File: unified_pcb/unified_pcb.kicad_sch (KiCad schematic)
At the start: 102 parts, among them J1 Conn_01x02_Socket, J2 USB_C_Receptacle, J3 Conn_01x02_Socket, J4 Conn_01x03_Pin, Q1 Q_Photo_NPN, Q2 Q_Photo_NPN, Q3 Q_Photo_NPN, SW1 SW_Push, SW2 SW_Push, U1 BQ27427YZFR, U10 3.3V LDO, U11 LMD4030T261-OA1, U12 LY4176D, U2 USBLC6-2P6, U3 RS0302, U4 RP2350_60QFN, U5 TLV7113318DDSER, U7 QSPI Flash, U8 TPGLF72101CSP4, U9 ICM-20948, Y1 12MHz

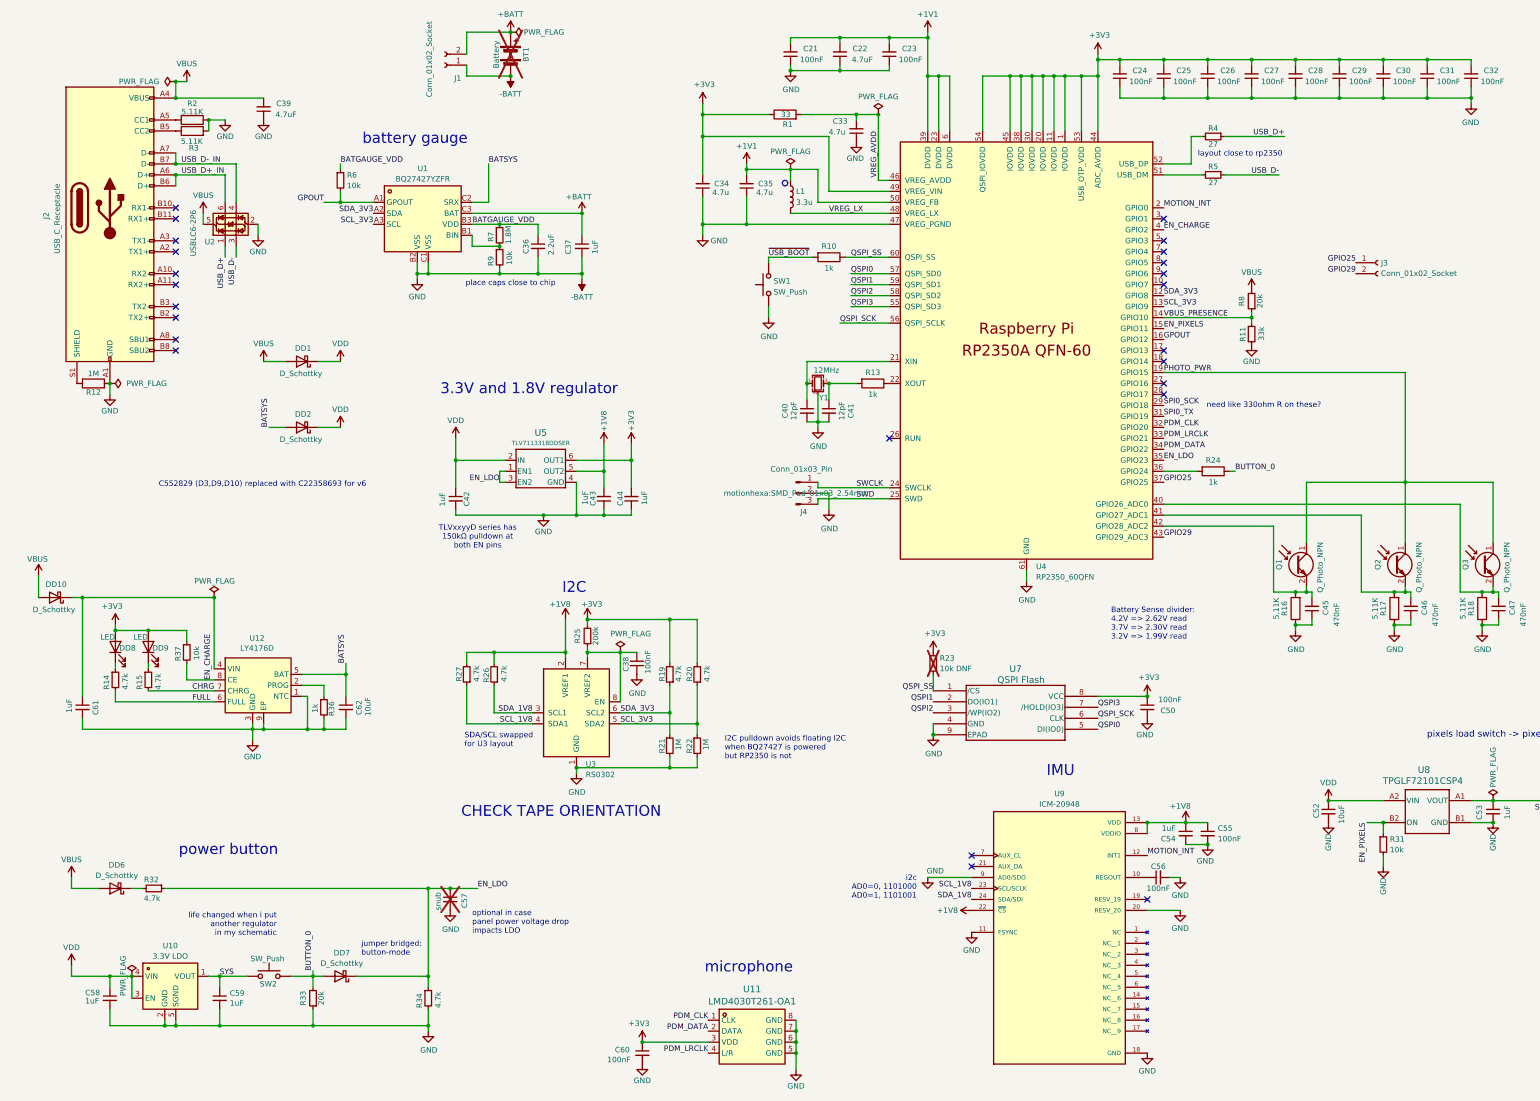
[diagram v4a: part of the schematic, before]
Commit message: wow ICM_20948 is moving out of production and is expensive - move to BMI270+MMC5603NJ, no need anymore for 1.8V net at all remove old schematic pieces, update schematic format mag layout fix crystal and other part nums
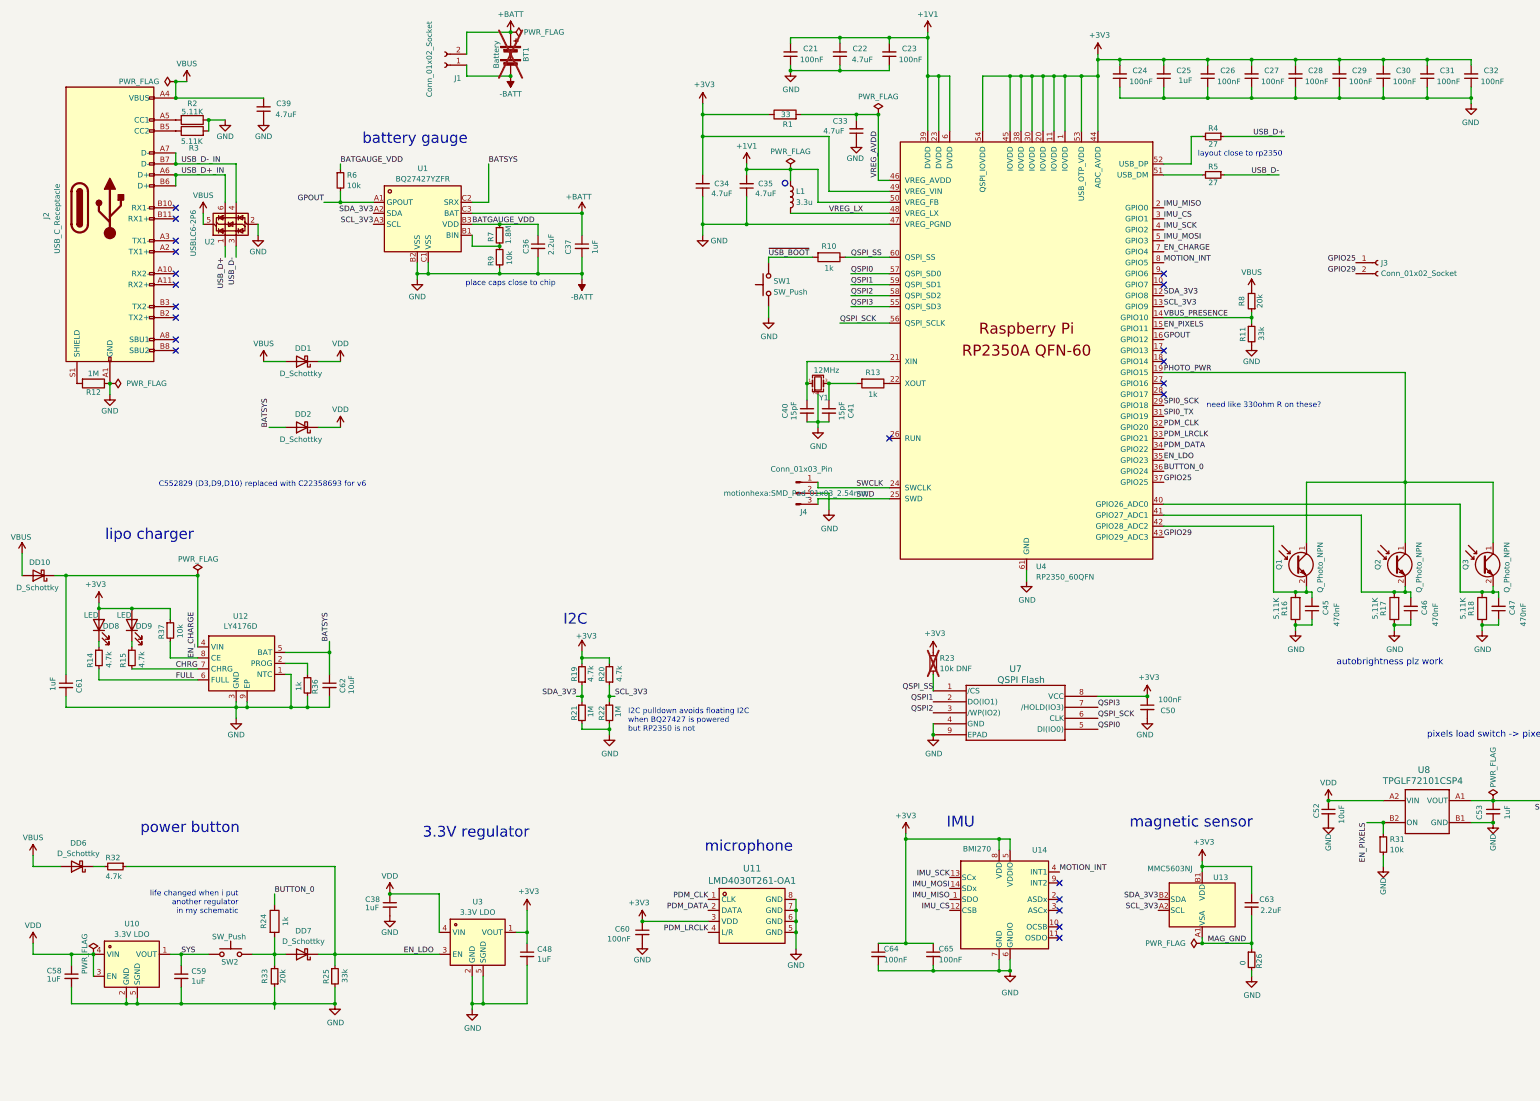
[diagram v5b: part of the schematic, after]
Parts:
- removed C42, C43, C44, C54: 1uF, Capacitor_SMD:C_0402_1005Metric, symbol Device:C_Small
- removed C55, C56: 100nF, Capacitor_SMD:C_0402_1005Metric, symbol Device:C_Small
- removed C57: snub, Capacitor_SMD:C_0402_1005Metric, symbol Device:C_Small
- removed R27, R34: 4.7k, Resistor_SMD:R_0402_1005Metric, symbol Device:R_Small
- removed U3: RS0302, Package_SON:X2SON-8_1.4x1mm_P0.35mm, symbol motionhexa:RS0302
- removed U5: TLV7113318DDSER, Package_SON:WSON-6_1.5x1.5mm_P0.5mm, symbol motionhexa:TLV7111833DDSER
- removed U9: ICM-20948, motionhexa:QFN40P300X300X105-24N, symbol motionhexa:ICM-20948
- added C48: 1uF, Capacitor_SMD:C_0402_1005Metric, symbol Device:C_Small
- added C63: 2.2uF, Capacitor_SMD:C_0402_1005Metric, symbol Device:C_Small
- added C64, C65: 100nF, Capacitor_SMD:C_0402_1005Metric, symbol Device:C_Small
- added U13: MMC5603NJ, motionhexa:MMC5603NJ_WLP-4_0.8x0.8mm_P0.4mm, symbol motionhexa:MMC5603NJ
- added U14: BMI270, Package_LGA:Bosch_LGA-14_3x2.5mm_P0.5mm, symbol motionhexa:BMI270
- added U3: 3.3V LDO, Package_DFN_QFN:OnSemi_XDFN4-1EP_1.0x1.0mm_EP0.52x0.52mm, symbol penta:RT9078-33GQZ
- C25, C38: value 100nF -> 1uF; Designation CC0402KRX7R7BB104 -> CL05A105KP5NNNC; LCSC C60474 -> C14445
- C33, C34, C35: value 4.7u -> 4.7uF
- C40, C41: value 12pF -> 15pF; Designation 0402N120F500CT -> 0402CG150J500NT; LCSC C555399 -> C1548
- C61: Designation (none) -> CL05A105KP5NNNC; LCSC (none) -> C14445
- C62: Designation (none) -> 0603X106K100; LCSC (none) -> C90806
- R14, R15, R19, R20, R32: Designation 0402WGF4701TCE -> FRC0402J472 TS; LCSC C25900 -> C2906941
- R16, R17, R18: Designation RC0402FR-07511KL -> RC0402FR-075K11L; LCSC C163461 -> C274895
- R25: value 200k -> 33k; Designation (none) -> 0402WGF3302TCE; LCSC (none) -> C25779
- R26: value 4.7k -> 0; Designation 0402WGF4701TCE -> 0402WGF0000TCE; LCSC C25900 -> C17168
- R36: Designation (none) -> RC0402FR-071KL; LCSC (none) -> C106235
- U1: LCSC Part C6075475 -> (none)
- U10: LCSC (none) -> C147954; LCSC Part C147954 -> (none)
- U4: JLC C42411118 -> (none); LCSC (none) -> C42411118
- U8: symbol motionhexa:TPS22913BYZVR -> motionhexa:TPGLF72101CSP4
- Y1: footprint Crystal:Crystal_SMD_2520-4Pin_2.5x2.0mm -> Crystal:Crystal_SMD_3225-4Pin_3.2x2.5mm; Designation TXM12M0004252FBCEO00T -> ABM8-272-T3; LCSC C284155 -> C20625731
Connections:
- net +1V8 is gone; now on net -BATT: R26.2
- net +3V3: now also C48.1, C63.1, C64.1, C65.1, U13.B1 (VDD), U14.5 (VDDIO), U14.8 (VDD), U3.1 (VOUT); no longer R25.2
- net -BATT: now also C38.2, R25.2, C48.2, C64.2, C65.2, U14.6 (GNDIO), U14.7 (GND), U3.2 (GND), U3.5 (SGND); no longer C38.1
- net BUTTON_0: now also U4.36 (GPIO24); no longer DD7.2 (A), R33.2, SW2.2
- net EN_CHARGE: now also U4.7 (GPIO4); no longer U4.4 (GPIO2)
- net EN_LDO: now also R25.1, U3.3 (EN)
- net MOTION_INT: now also U4.8 (GPIO5), U14.4 (INT1); no longer U4.2 (GPIO0)
- net SCL_3V3: now also U13.A2 (SCL)
- net SDA_3V3: now also U13.B2 (SDA)
- net VDD: now also C38.1, U3.4 (VIN)
- net at R24.2: now also DD7.2 (A), R33.2, SW2.2; no longer U4.36 (GPIO24)
- net IMU_CS: now reaches U4.3 (GPIO1)
- net IMU_CS: now also U14.12 (CSB)
- net IMU_MOSI: now reaches U4.5 (GPIO3)
- net IMU_MOSI: now also U14.14 (SDx)
- net SDA_1V8 renamed MAG_GND
- net MAG_GND: now also C63.2, U13.A1 (VSA)
- new net IMU_MISO: U14.1 (SDO), U4.2 (GPIO0)
- new net IMU_SCK: U14.13 (SCx), U4.4 (GPIO2)
- no-connect marks 24 -> 22
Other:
- note added: "3.3V regulator"
- note added: "autobrightness plz work"
- note added: "lipo charger"
- note added: "magnetic sensor"
- note removed: "3.3V and 1.8V regulator"
- note removed: "Battery Sense divider: 4.2V => 2.62V read 3.7V => 2.30V read 3.2V => 1.99V read"
- note removed: "CHECK TAPE ORIENTATION"
- note removed: "SDA/SCL swapped for U3 layout"
- note removed: "TLVxxyyD series has 150kΩ pulldown at both EN pins"
- note removed: "i2c AD0=0, 1101000 AD0=1, 1101001"
- note removed: "jumper bridged: button-mode"
- note removed: "optional in case panel power voltage drop impacts LDO"
- moved on the sheet: C58, C59, C60, C61, C62, DD10, DD6, DD7, DD8, DD9, R14, R15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

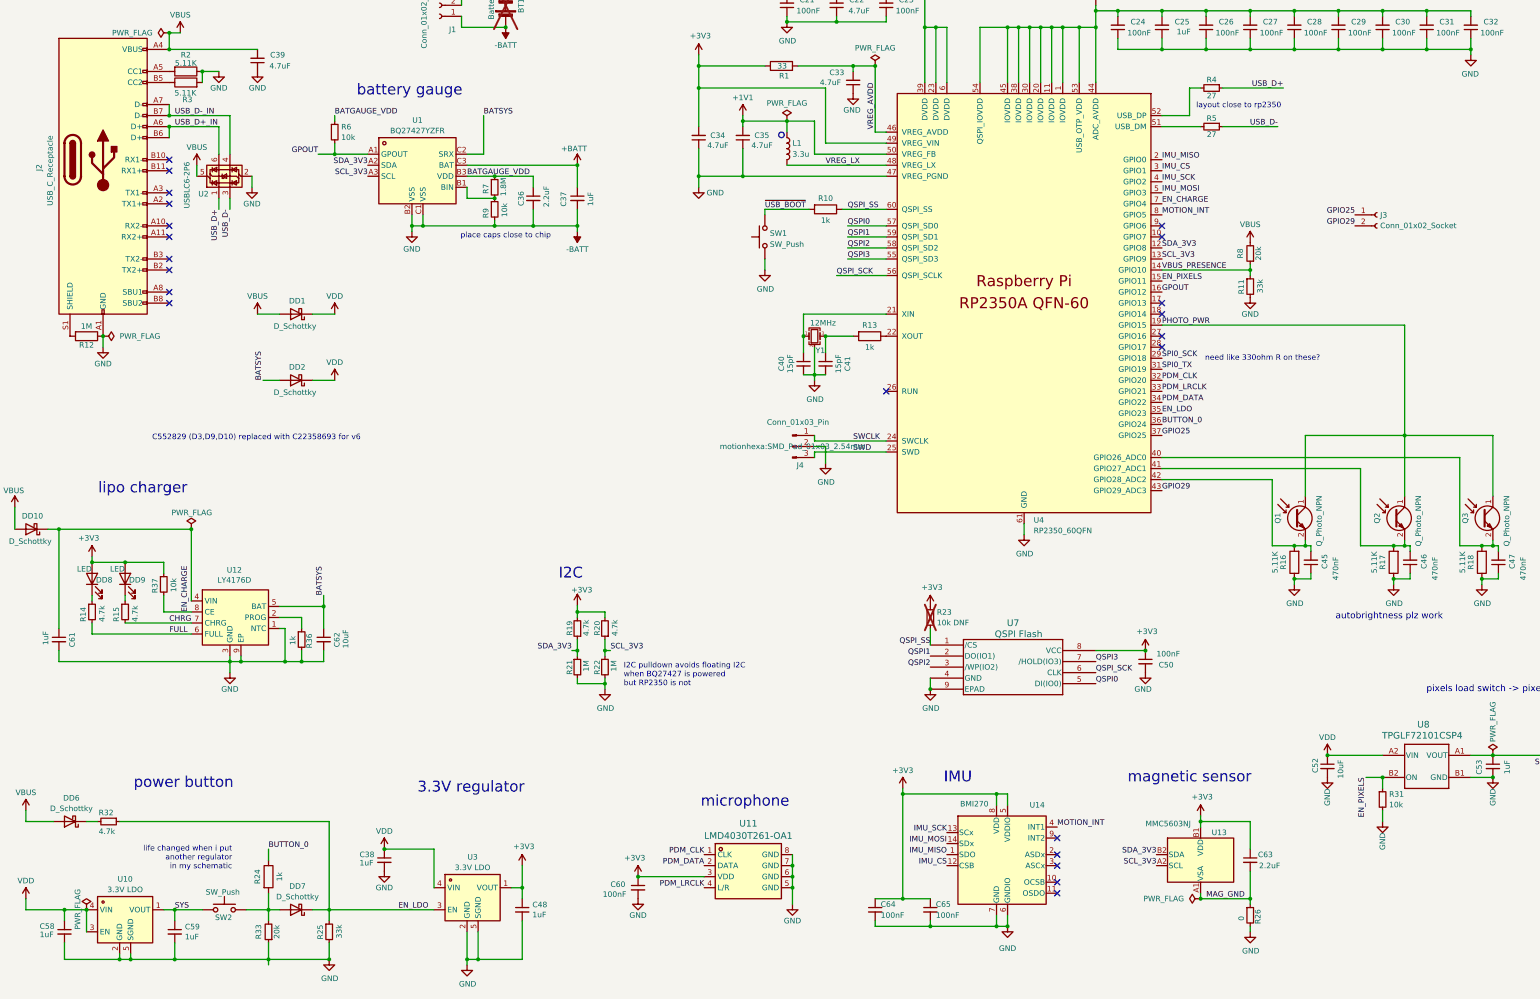
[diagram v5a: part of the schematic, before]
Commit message: magnetic sensor layout in a little corner of the board hopefully well isolated
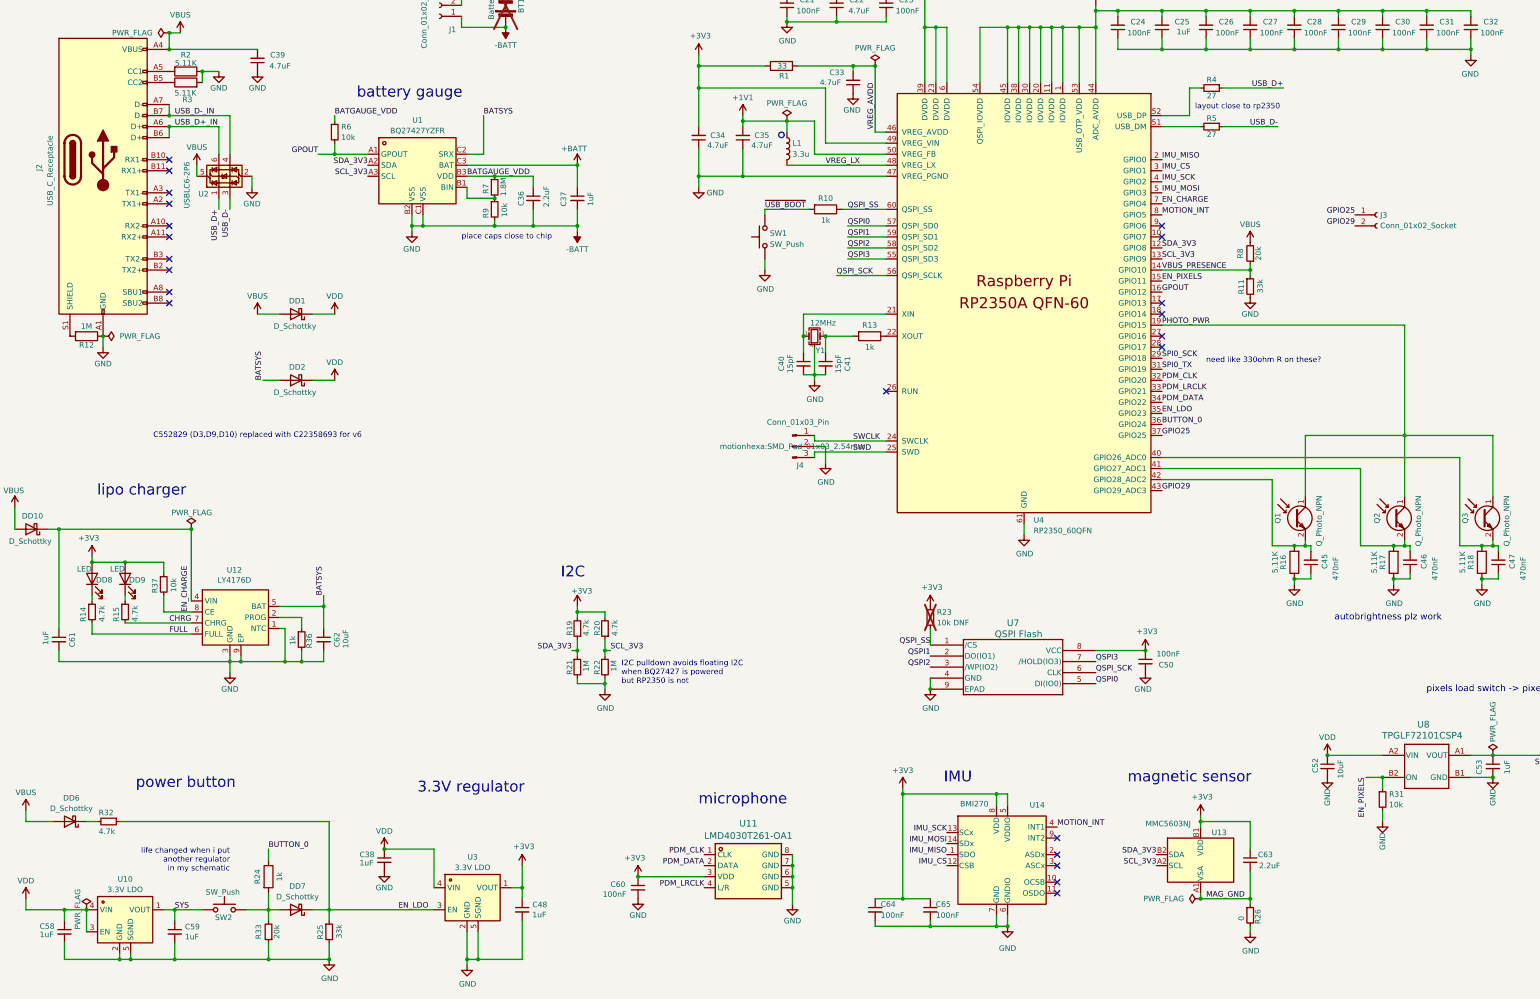
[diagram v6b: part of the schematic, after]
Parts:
- U3: symbol penta:RT9078-33GQZ -> motionhexa:RT9078-33GQZ
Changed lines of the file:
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@@
 	(text "lipo charger"
 		(exclude_from_sim no)
-		(at 49.784 144.272 0)
+		(at 49.53 144.78 0)
 		(effects
 			(font
@@
 	(text "life changed when i put\nanother regulator\nin my schematic"
 		(exclude_from_sim no)
-		(at 70.358 229.362 0)
+		(at 69.85 229.87 0)
 		(effects
 			(font
@@
 	(text "I2C pulldown avoids floating I2C\nwhen BQ27427 is powered\nbut RP2350 is not"
 		(exclude_from_sim no)
-		(at 160.528 187.198 0)
+		(at 160.02 186.69 0)
 		(effects
 			(font
@@
 	(text "need like 330ohm R on these?"
 		(exclude_from_sim no)
-		(at 294.386 115.062 0)
+		(at 294.64 115.57 0)
 		(effects
 			(font
@@
 	(text "C552829 (D3,D9,D10) replaced with C22358693 for v6"
 		(exclude_from_sim no)
-		(at 75.946 132.588 0)
+		(at 76.2 132.08 0)
 		(effects
 			(font
@@
 	(text "battery gauge"
 		(exclude_from_sim no)
-		(at 99.06 54.102 0)
+		(at 99.06 54.61 0)
 		(effects
 			(font
@@
 	(text "microphone"
 		(exclude_from_sim no)
-		(at 188.468 216.408 0)
+		(at 187.96 215.9 0)
 		(effects
 			(font
@@
 	(text "place caps close to chip"
 		(exclude_from_sim no)
-		(at 122.936 86.106 0)
+		(at 123.19 86.36 0)
 		(effects
 			(font
@@
 	(text "power button"
 		(exclude_from_sim no)
-		(at 59.182 212.09 0)
+		(at 59.69 212.09 0)
 		(effects
 			(font
@@
 	(text "layout close to rp2350"
 		(exclude_from_sim no)
-		(at 292.354 56.896 0)
+		(at 292.1 57.15 0)
 		(effects
 			(font
@@
 	(text "autobrightness plz work"
 		(exclude_from_sim no)
-		(at 336.804 173.736 0)
+		(at 336.55 173.99 0)
 		(effects
 			(font
@@
 	(text "I2C"
 		(exclude_from_sim no)
-		(at 145.542 165.354 0)
+		(at 146.05 165.1 0)
 		(effects
 			(font
@@
 	(wire
 		(pts
-			(xy 78.74 252.73) (xy 78.74 254)
-		)
-		(stroke
-			(width 0)
-			(type default)
-		)
-	)
-	(wire
-		(pts
 			(xy 36.83 241.3) (xy 36.83 246.38)
 		)
@@
 	(wire
 		(pts
-			(xy 149.86 171.196) (xy 149.86 172.72)
+			(xy 149.86 171.45) (xy 149.86 172.72)
 		)
 		(stroke
@@
 	)
 	(symbol
-		(lib_id "penta:RT9078-33GQZ")
+		(lib_id "motionhexa:RT9078-33GQZ")
 		(at 125.73 238.76 0)
 		(unit 1)
@@
 	(symbol
 		(lib_id "power:+3V3")
-		(at 149.86 171.196 0)
+		(at 149.86 171.45 0)
 		(unit 1)
 		(exclude_from_sim no)
@@
 		(dnp no)
 		(property "Reference" "#PWR020"
-			(at 149.86 175.006 0)
+			(at 149.86 175.26 0)
 			(effects
 				(font
@@
 		)
 		(property "Value" "+3V3"
-			(at 150.876 167.64 0)
+			(at 150.876 167.894 0)
 			(effects
 				(font
@@
 		)
 		(property "Footprint" ""
-			(at 149.86 171.196 0)
+			(at 149.86 171.45 0)
 			(effects
 				(font
@@
 		)
 		(property "Datasheet" ""
-			(at 149.86 171.196 0)
+			(at 149.86 171.45 0)
 			(effects
 				(font
@@
 		)
 		(property "Description" "Power symbol creates a global label with name \"+3V3\""
-			(at 149.86 171.196 0)
+			(at 149.86 171.45 0)
 			(effects
 				(font
